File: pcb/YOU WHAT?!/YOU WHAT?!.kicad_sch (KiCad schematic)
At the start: 20 parts, among them J1 Conn_01x04, Q1 BC849C, U1 4069

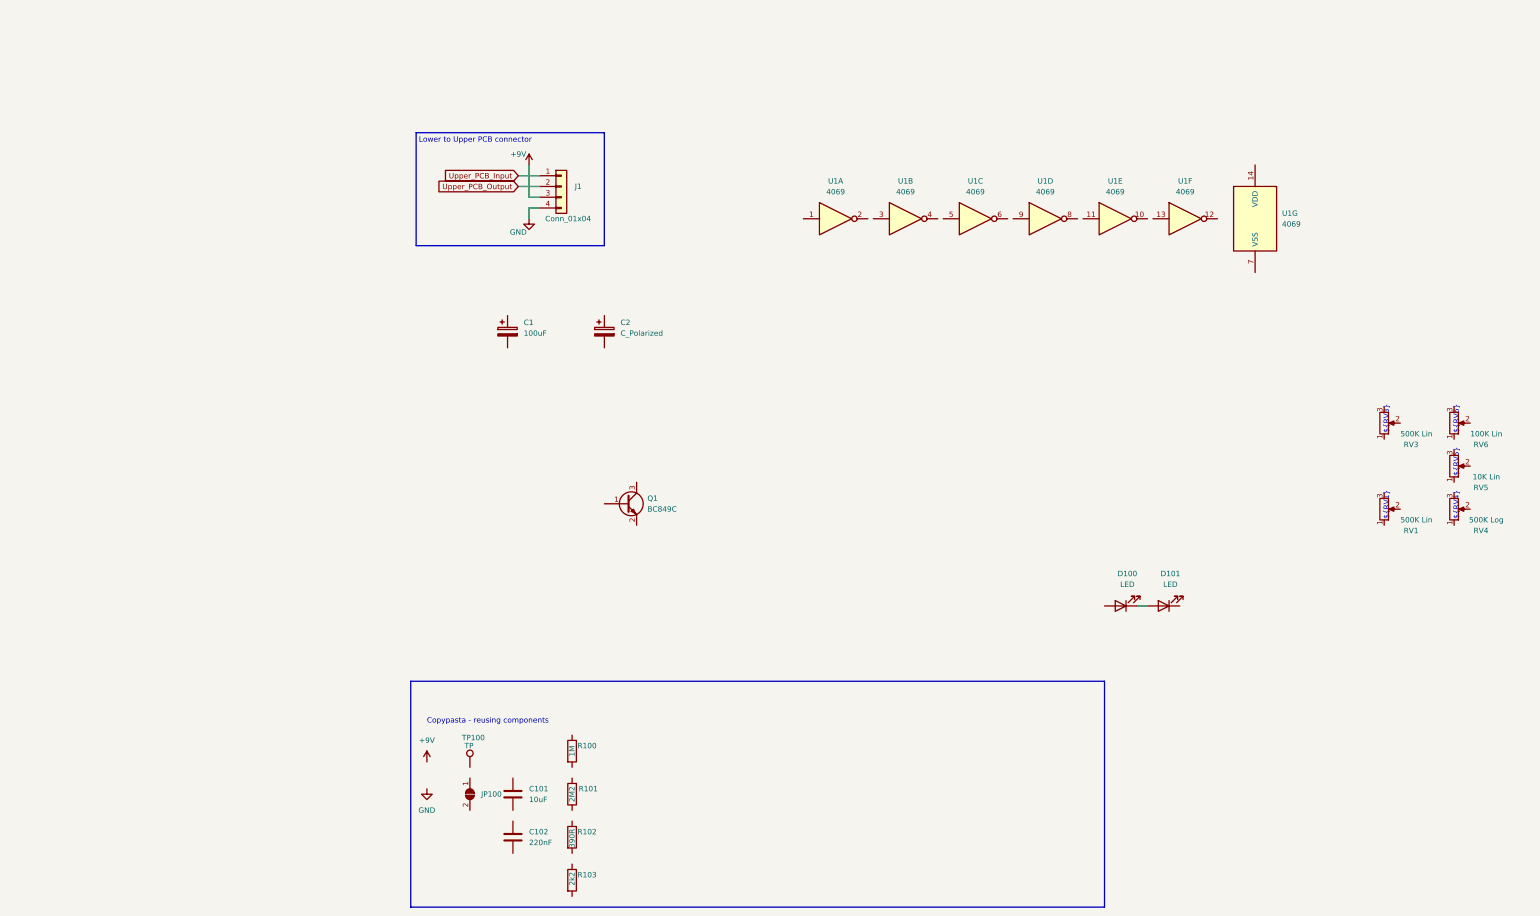
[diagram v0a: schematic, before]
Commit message: [YW] Add all devices to schematic and start wiring
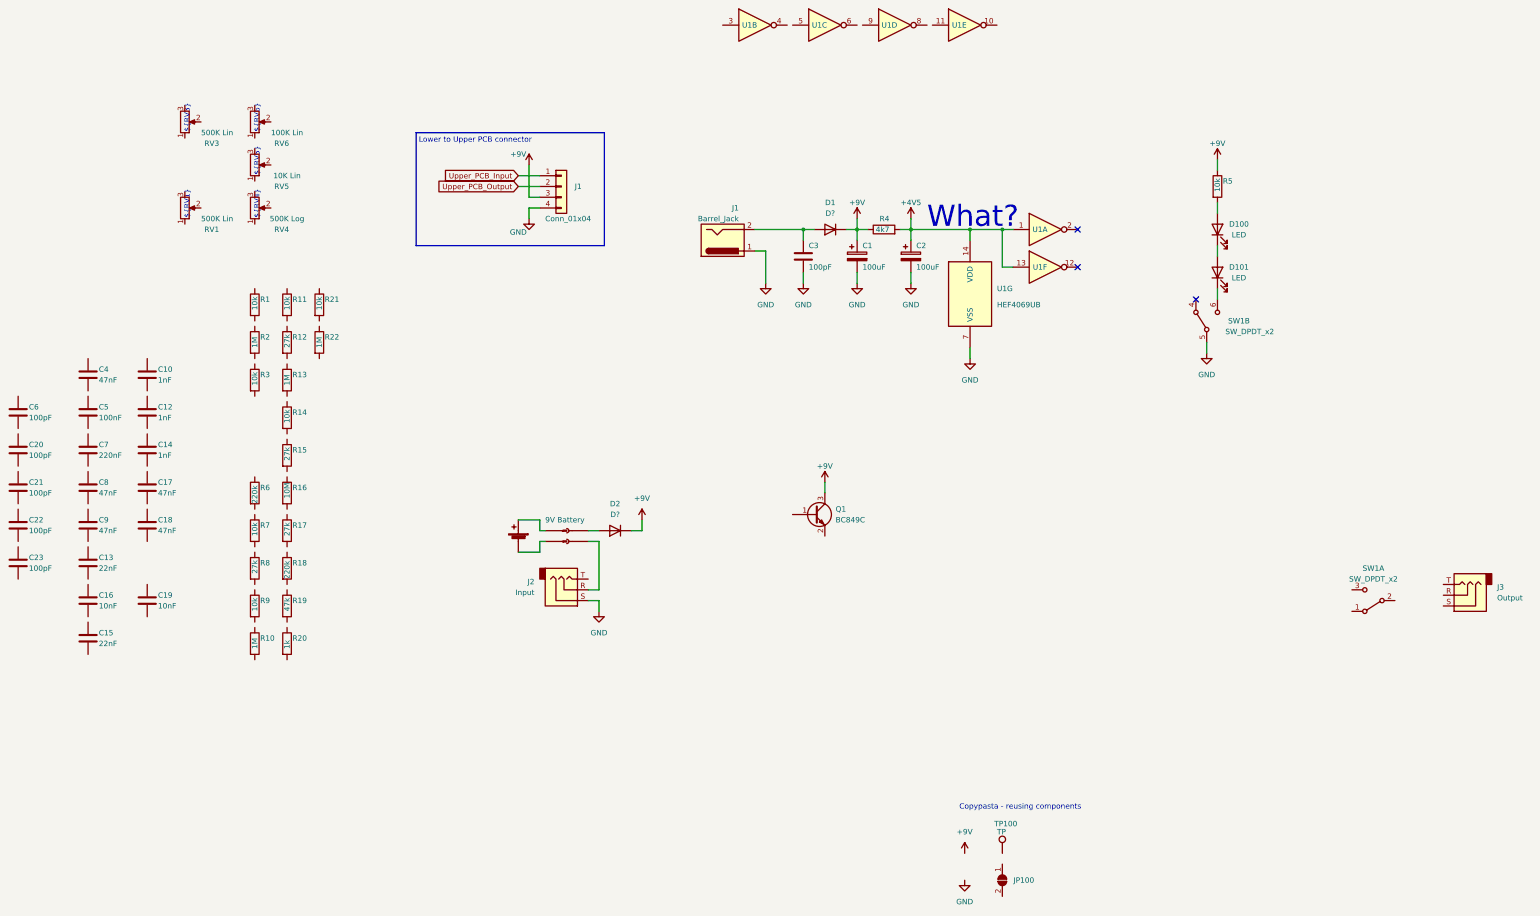
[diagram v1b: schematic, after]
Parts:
- removed C101: 10uF, Capacitor_SMD:C_0805_2012Metric, symbol Device:C
- removed C102: 220nF, Capacitor_SMD:C_0603_1608Metric, symbol Device:C
- removed R101: 2M2, Resistor_SMD:R_0603_1608Metric, symbol Device:R
- removed R102: 390R, Resistor_SMD:R_0603_1608Metric, symbol Device:R
- removed R103: 2k2, Resistor_SMD:R_0603_1608Metric, symbol Device:R
- added BT1: 9V Battery, symbol Device:Battery_Cell
- added C10, C12, C14: 1nF, symbol Device:C
- added C13, C15: 22nF, symbol Device:C
- added C16, C19: 10nF, symbol Device:C
- added C17, C18, C4, C8, C9: 47nF, symbol Device:C
- added C20, C21, C22, C23, C3, C6: 100pF, symbol Device:C
- added C5: 100nF, symbol Device:C
- added C7: 220nF, symbol Device:C
- added D1, D2: D?, symbol Device:D
- added J1: Barrel_Jack, symbol Connector:Barrel_Jack
- added J101: Conn_01x02_Male, symbol Connector:Conn_01x02_Male
- added J102: 9V Battery, symbol Connector:Conn_01x02_Female
- added J2: Input, symbol Connector:AudioJack3
- added J3: Output, symbol Connector:AudioJack3
- added R1, R11, R14, R21, R3, R5, R7, R9: 10k, Resistor_SMD:R_0603_1608Metric, symbol Device:R
- added R10, R13, R2: 1M, Resistor_SMD:R_0603_1608Metric, symbol Device:R
- added R12, R15, R17, R8: 27k, Resistor_SMD:R_0603_1608Metric, symbol Device:R
- added R16: 10M, Resistor_SMD:R_0603_1608Metric, symbol Device:R
- added R18, R6: 220k, Resistor_SMD:R_0603_1608Metric, symbol Device:R
- added R19: 47k, Resistor_SMD:R_0603_1608Metric, symbol Device:R
- added R20: 1k, Resistor_SMD:R_0603_1608Metric, symbol Device:R
- added R4: 4k7, Resistor_SMD:R_0603_1608Metric, symbol Device:R
- added SW1: SW_DPDT_x2, symbol Switch:SW_DPDT_x2
- C2: value C_Polarized -> 100uF
- U1: value 4069 -> HEF4069UB
- renumbered R100 to R22
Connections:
- net +9V: now also C1.1, Q1.3 (C), D1.1 (K), D2.1 (K), R4.1, R5.1
- net GND: now also C1.2, C2.2, U1.7 (VSS), C3.2, J1.1, J2.S, SW1.5 (B)
- net +4V5: now reaches C2.1
- net +4V5: now also U1.1, U1.13, U1.14 (VDD), R4.2
- net at D100.2 (A): now also R5.2
- net at D101.1 (K): now also SW1.6 (C)
- new net: BT1.1 (+), J101.2 (Pin_2)
- new net: BT1.2 (-), J101.1 (Pin_1)
- new net: J102.1 (Pin_1), J2.R
- new net: D2.2 (A), J102.2 (Pin_2)
- new net: C3.1, D1.2 (A), J1.2
- no-connect marks 0 -> 3
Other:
- note added: "What?"
- moved on the sheet: C1, C2, D100, D101, JP100, Q1, R22, RV1, RV3, RV4, RV5, RV6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

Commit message: [YW] Continue reverse engineering
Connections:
- net +4V5: now also R22.1
- net GND: now also C18.2, C6.2, R2.2, R3.2
- net at R20.1: now also R17.1, R18.1
- net at R20.2: now also C18.1
- net at C16.1: now also C23.2, R17.2, U1.8
- net at C16.2: now also R14.1
- net at R13.1: now also C20.1, R21.2, U1.3
- net at R13.2: now also C20.2, R12.2, U1.4
- net at C23.1: now also R18.2, R19.1, U1.9
- net at SW1.1 (A): now also C5.2, R2.1
- net at SW1.2 (B): now also J3.T
- net at R3.1: now also C17.1, C5.1, Q1.2 (E)
- net at C6.1: now also C4.1, R1.2
- net at C19.1: now also RV1.3
- net at C19.2: now also R21.1
- net at C4.2: now also Q1.1 (B), R22.2
- net at C22.1: now also R14.2, R15.1, U1.11
- net at C22.2: now also R16.2, RV1.2, U1.10
- net at R19.2: now also C17.2
- net at J2.T: now also R1.1
- net at C15.1: now also RV1.1
- net at C15.2: now also R15.2, R16.1
- no-connect marks 3 -> 5
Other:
- note removed: "Copypasta - reusing components"
- moved on the sheet: C1, C15, C16, C17, C18, C19, C2, C20, C21, C22, C23, C3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

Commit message: [YW] Finish initial routing of schematic
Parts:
- added C11: 220nF, symbol Device:C
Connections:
- net GND: now also C12.2, C13.2, C14.2, R10.2, RV5.1
- net at R6.1: now also C21.1, RV3.1, U1.5
- net at R6.2: now also C7.2
- net at C8.1: now also C9.1, R8.2
- net at C8.2: now also RV5.2
- net at U1.6: now also C21.2, R7.1, C11.1
- net at R8.1: now also C10.1, C14.1, R11.1, R12.1
- net at C12.1: now also R10.1, R9.2, SW1.3 (C)
- net at RV5.3: now also RV4.1
- net at C10.2: now also RV6.3
- net at R11.2: now also C13.1
- net at R9.1: now also C11.2
- net at C9.2: now also RV4.2, RV4.3, RV6.1
- net at C7.1: now also RV6.2
- net at R7.2: now also RV3.2, RV3.3
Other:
- moved on the sheet: C10, C12, C13, C14, C21, C7, C8, C9, R10, R11, R6, R7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

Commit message: [YW] Schematic beautification before modifying
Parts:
- C20, C21, C22, C23, C3, C6: value 100pF -> 47pF
- C5: value 100nF -> 220nF
- D1, D2: value D? -> Any 0.6V
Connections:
- net GND: now also J3.R, J3.S
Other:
- note added: "Empty footprint"
- note added: "~800uA current draw from 4V5 --> ~4V drop over R4 --> in ~4.4V bias voltage"
- note removed: "What?"
- moved on the sheet: C1, C10, C11, C12, C13, C14, C15, C16, C17, C18, C19, C2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

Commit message: [YW] Remove n. required stuff from schematic and modify to fit system
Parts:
- removed BT1: 9V Battery, symbol Device:Battery_Cell
- removed C1: 100uF, symbol Device:C_Polarized
- removed C3: 47pF, symbol Device:C
- removed C5: 220nF, symbol Device:C
- removed D1, D2: Any 0.6V, symbol Device:D
- removed D100, D101: LED, symbol Device:LED
- removed J1: Barrel_Jack, symbol Connector:Barrel_Jack
- removed J101: Conn_01x02_Male, symbol Connector:Conn_01x02_Male
- removed J102: 9V Battery, symbol Connector:Conn_01x02_Female
- removed J2: Input, symbol Connector:AudioJack3
- removed J3: Output, symbol Connector:AudioJack3
- removed JP100: Jmp, Jumper:SolderJumper-2_P1.3mm_Open_TrianglePad1.0x1.5mm, symbol Jumper:SolderJumper_2_Open
- removed R10, R2: 1M, Resistor_SMD:R_0603_1608Metric, symbol Device:R
- removed R5: 10k, Resistor_SMD:R_0603_1608Metric, symbol Device:R
- removed SW1: SW_DPDT_x2, symbol Switch:SW_DPDT_x2
- removed TP100: TP, TestPoint:TestPoint_Pad_D2.0mm, symbol Connector:TestPoint
- added TP1: PostInp, TestPoint:TestPoint_Pad_D2.0mm, symbol Connector:TestPoint
- added TP2: 9V, TestPoint:TestPoint_Pad_D2.0mm, symbol Connector:TestPoint
- added TP3: 4V5, TestPoint:TestPoint_Pad_D2.0mm, symbol Connector:TestPoint
- added TP4: PostGain, TestPoint:TestPoint_Pad_D2.0mm, symbol Connector:TestPoint
- added TP5: PostTone, TestPoint:TestPoint_Pad_D2.0mm, symbol Connector:TestPoint
- C10, C12, C14: footprint (none) -> Capacitor_SMD:C_0603_1608Metric; LCSC (none) -> C1588
- C11, C7: footprint (none) -> Capacitor_SMD:C_0603_1608Metric
- C13, C15: footprint (none) -> Capacitor_SMD:C_0603_1608Metric; LCSC (none) -> C21122
- C16, C19: footprint (none) -> Capacitor_SMD:C_0603_1608Metric; LCSC (none) -> C57112
- C17, C18, C4, C8, C9: footprint (none) -> Capacitor_SMD:C_0603_1608Metric; LCSC (none) -> C1622
- C2: footprint (none) -> Capacitor_THT:CP_Radial_D5.0mm_P2.00mm; LCSC (none) -> C108360
- C20, C21, C22, C23, C6: footprint (none) -> Capacitor_SMD:C_0603_1608Metric; LCSC (none) -> C1671
- R1, R11, R14, R21, R3, R7, R9: LCSC (none) -> C25804
- R12, R15, R17, R8: LCSC (none) -> C22967
- R13, R22: LCSC (none) -> C22935
- R16: LCSC (none) -> C7250
- R18, R6: LCSC (none) -> C17556
- R19: LCSC (none) -> C25819
- R20: LCSC (none) -> C21190
- R4: LCSC (none) -> C23162
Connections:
- net +4V5: now also TP3.1
- net +9V: now also TP2.1
- net Upper_PCB_Input: now also R1.1
- net Upper_PCB_Output: now also C12.1, R9.2
- net at C17.1, Q1.2 (E), R3.1: now also TP1.1
- net at C19.1, RV1.3: now also TP4.1
- net at C7.1, RV6.2: now also TP5.1
- no-connect marks 5 -> 2
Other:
- note removed: "Empty footprint"
- title: PedalDev_UpperRaw -> YOU WHAT?!
- moved on the sheet: C2, C4, C6, Q1, R1, R22, R3, R4, U1A, U1F, U1G

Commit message: [YW] Start creating PCB
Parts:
- C2: footprint Capacitor_THT:CP_Radial_D5.0mm_P2.00mm -> Capacitor_SMD:CP_Elec_6.3x5.3; LCSC C108360 -> C134723
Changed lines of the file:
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@@
       (effects (font (size 1.27 1.27)) (justify left))
     )
-    (property "Footprint" "Capacitor_THT:CP_Radial_D5.0mm_P2.00mm" (id 2) (at 133.0452 77.47 0)
+    (property "Footprint" "Capacitor_SMD:CP_Elec_6.3x5.3" (id 2) (at 133.0452 77.47 0)
       (effects (font (size 1.27 1.27)) hide)
     )
@@
       (effects (font (size 1.27 1.27)) hide)
     )
-    (property "LCSC" "C108360" (id 4) (at 132.08 73.66 0)
+    (property "LCSC" "C134723" (id 4) (at 132.08 73.66 0)
       (effects (font (size 1.27 1.27)) hide)
     )
@@
     )
     (path "/331fd5fb-32ab-404a-bd96-618aec4f919d"
-      (reference "C2") (unit 1) (value "100uF") (footprint "Capacitor_THT:CP_Radial_D5.0mm_P2.00mm")
+      (reference "C2") (unit 1) (value "100uF") (footprint "Capacitor_SMD:CP_Elec_6.3x5.3")
     )
     (path "/4dde8892-41e8-436e-83f9-e71b85a67f48"
